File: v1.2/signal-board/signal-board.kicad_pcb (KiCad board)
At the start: 4 copper layers, 73 x 43 mm, 47 parts, among them IC1 74HCT245, J1 Jack-DC, J2 Conn_01x12, J3 JST SM, J4 Conn_01x16, J5 switch_jumpers, J6 switch_jumpers, SW1 SW_MEC_5G, SW2 SW_MEC_5G, U1 TPS63060, U2 ESP32-DEVKITC-32D

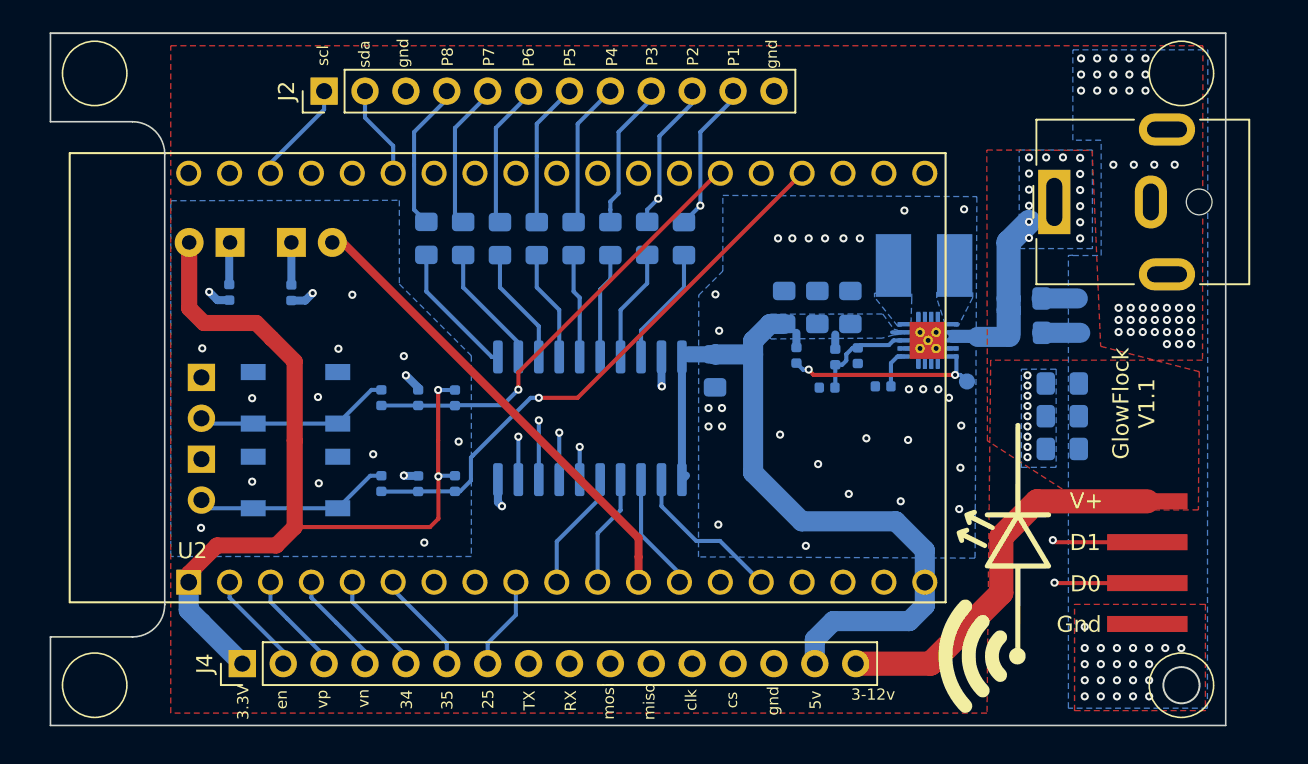
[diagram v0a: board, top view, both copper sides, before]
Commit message: added holes to corners
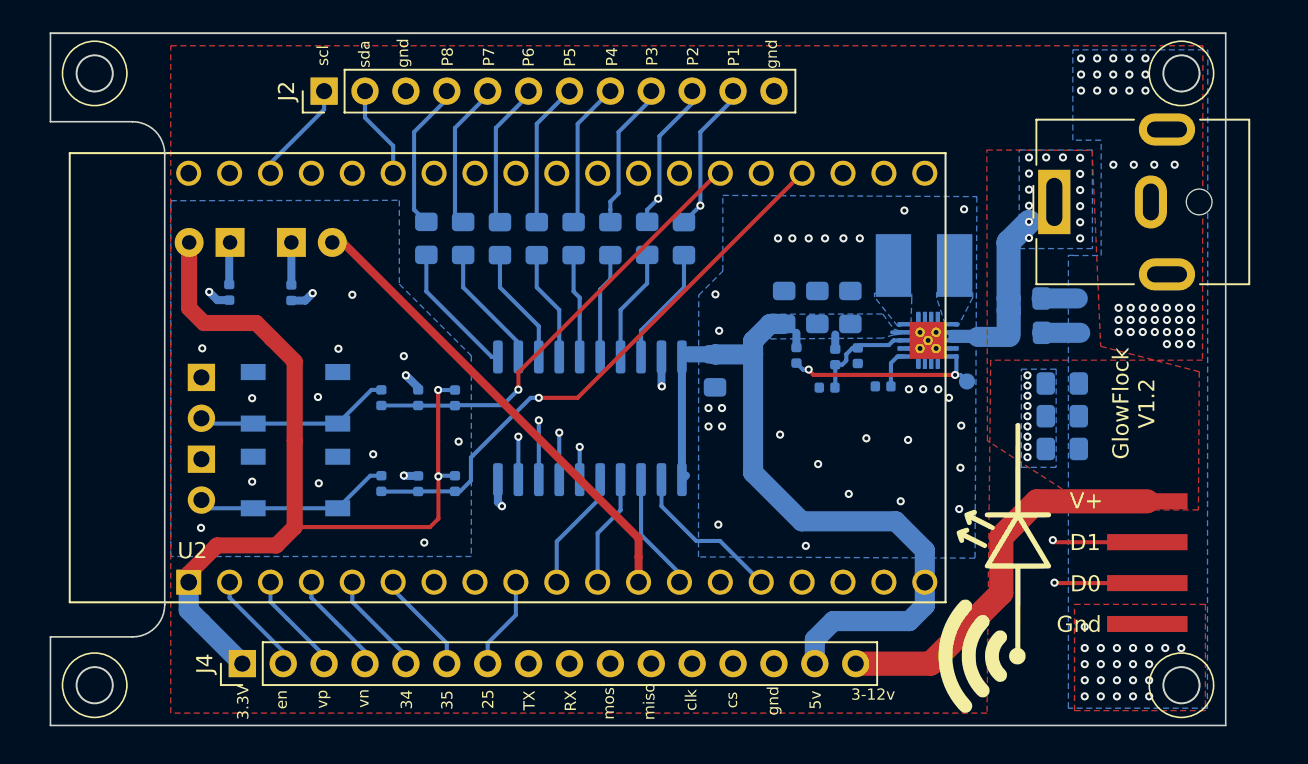
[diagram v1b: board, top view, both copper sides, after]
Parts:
- R1: value 1K -> 1M
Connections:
- U2 pad 16: Net-(U2-Pad16) -> (no net)
- U2 pad 17: Net-(U2-Pad17) -> (no net)
- U2 pad 18: Net-(U2-Pad18) -> (no net)
- U2 pad 36: Net-(U2-Pad36) -> (no net)
- U2 pad 37: Net-(U2-Pad37) -> (no net)
- U2 pad 38: Net-(U2-Pad38) -> (no net)
- U2 pad 7: Net-(U2-Pad7) -> (no net)
- U2 pad 8: Net-(U2-Pad8) -> (no net)
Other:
- outline, holes or cut-outs redrawn
- board text added: "GlowFlock V1.2"
- board text removed: "GlowFlock V1.1"

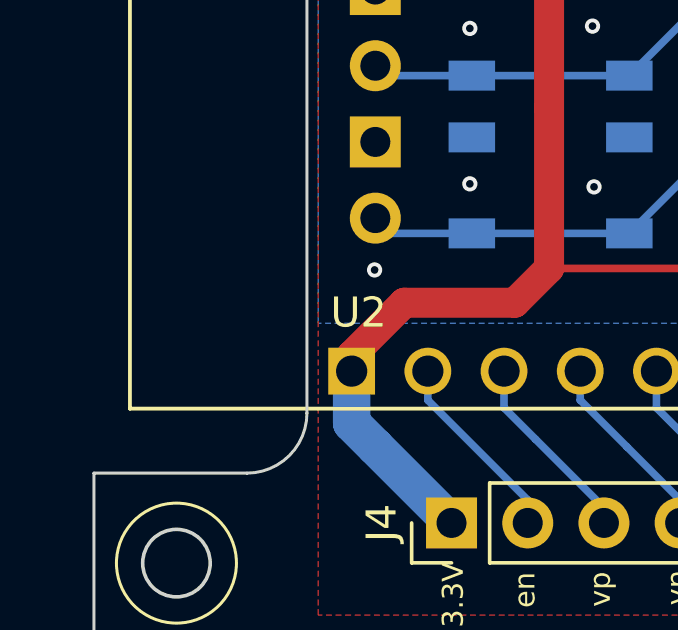
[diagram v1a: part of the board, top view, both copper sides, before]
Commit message: updated symbol and footprint links
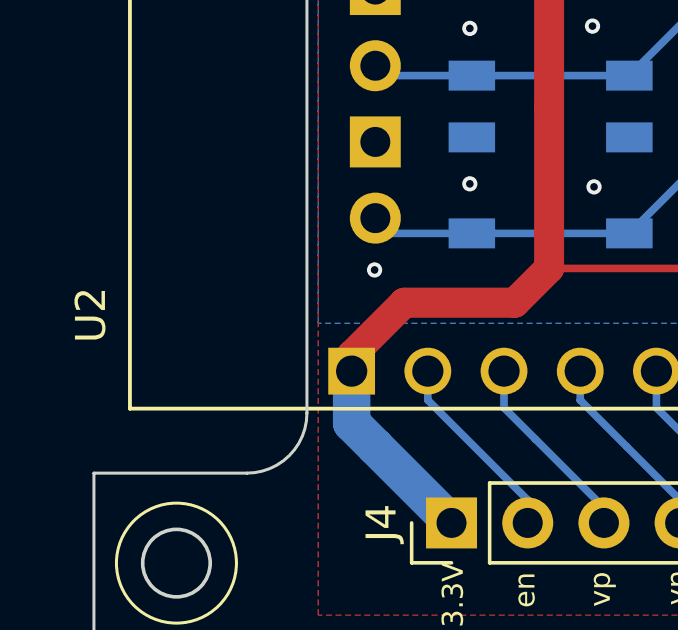
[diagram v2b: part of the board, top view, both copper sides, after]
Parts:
- IC1: footprint 74HCT245:SOIC-20W_7.5x10.0mm_P1.27mm -> GlowFlock footprints:SOIC-20W_7.5x10.0mm_P1.27mm
- SW1, SW2: footprint PTS 647:PTS647SK38SMTR2LFS -> GlowFlock footprints:PTS647SK38SMTR2LFS
- U2: footprint ESP32-DEVKITC-32D:MODULE_ESP32-DEVKITC-32D -> GlowFlock footprints:MODULE_ESP32-DEVKITC-32D
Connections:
- U2 pad 16: (no net) -> Net-(U2-Pad16)
- U2 pad 17: (no net) -> Net-(U2-Pad17)
- U2 pad 18: (no net) -> Net-(U2-Pad18)
- U2 pad 36: (no net) -> Net-(U2-Pad36)
- U2 pad 37: (no net) -> Net-(U2-Pad37)
- U2 pad 38: (no net) -> Net-(U2-Pad38)
- U2 pad 7: (no net) -> Net-(U2-Pad7)
- U2 pad 8: (no net) -> Net-(U2-Pad8)

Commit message: cleanup, new plug
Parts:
- J1: value Jack-DC -> DC Jack - PJ-002AH; footprint Connector_BarrelJack:BarrelJack_CUI_PJ-063AH_Horizontal -> GlowFlock footprints:CUI_PJ-002AH
- turned J1 to 0 degrees
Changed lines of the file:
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@@
   (net 61 "Net-(U2-Pad8)")
   (net 62 "Net-(U2-Pad7)")
+  (net 63 "Net-(J1-Pad3)")
   (module "Connector_PinHeader_2.54mm:PinHeader_1x16_P2.54mm_Vertical" locked (layer "F.Cu")
     (at 109.22 137.16 90)
@@
       (rotate (xyz 0 0 0))
     )
+  )
+  (module "GlowFlock footprints:CUI_PJ-002AH" (layer "F.Cu")
+    (at 159.675 108.475)
+    (property "MANUFACTURER" "CUI INC")
+    (property "STANDARD" "Manufacturer recommendations")
+    (property "Sheet file" "/e_drive/GlowFlock/v1.2/signal-board/signal-board.kicad_sch")
+    (property "Sheet name" "")
+    (attr through_hole)
+    (fp_text reference "J1" (at 2.485118 -6.76532) (layer "F.SilkS")
+      (effects (font (size 1.000047 1.000047) (thickness 0.015)))
+    )
+    (fp_text value "DC Jack - PJ-002AH" (at 6.939165 5.78266) (layer "F.Fab")
+      (effects (font (size 1.001323 1.001323) (thickness 0.015)))
+    )
+    (fp_line (start 13.7 4.5) (end -0.7 4.5) (layer "F.SilkS") (width 0.127))
+    (fp_line (start 13.7 -4.5) (end 13.7 4.5) (layer "F.SilkS") (width 0.127))
+    (fp_line (start -0.7 4.5) (end -0.7 2.65) (layer "F.SilkS") (width 0.127))
+    (fp_line (start -0.7 -2.55) (end -0.7 -4.5) (layer "F.SilkS") (width 0.127))
+    (fp_line (start 5.55 -4.5) (end 13.7 -4.5) (layer "F.SilkS") (width 0.127))
+    (fp_line (start -0.7 -4.5) (end 0.45 -4.5) (layer "F.SilkS") (width 0.127))
+    (fp_circle (center -2 0) (end -1.8 0) (layer "F.SilkS") (width 0.4))
+    (fp_line (start -1.55 2.35) (end -1 2.35) (layer "F.CrtYd") (width 0.05))
+    (fp_line (start 5.55 -4.75) (end 14 -4.75) (layer "F.CrtYd") (width 0.05))
+    (fp_line (start -1 -4.75) (end 0.45 -4.75) (layer "F.CrtYd") (width 0.05))
+    (fp_line (start 5.55 -6.1) (end 5.55 -4.75) (layer "F.CrtYd") (width 0.05))
+    (fp_line (start -1 4.75) (end -1 2.35) (layer "F.CrtYd") (width 0.05))
+    (fp_line (start 14 4.75) (end -1 4.75) (layer "F.CrtYd") (width 0.05))
+    (fp_line (start -1.55 -2.25) (end -1.55 2.35) (layer "F.CrtYd") (width 0.05))
+    (fp_line (start 0.45 -6.1) (end 5.55 -6.1) (layer "F.CrtYd") (width 0.05))
+    (fp_line (start 14 -4.75) (end 14 4.75) (layer "F.CrtYd") (width 0.05))
+    (fp_line (start 0.45 -4.75) (end 0.45 -6.1) (layer "F.CrtYd") (width 0.05))
+    (fp_line (start -1 -2.25) (end -1 -4.75) (layer "F.CrtYd") (width 0.05))
+    (fp_line (start -1 -2.25) (end -1.55 -2.25) (layer "F.CrtYd") (width 0.05))
+    (fp_line (start -0.7 4.5) (end -0.7 -4.5) (layer "F.Fab") (width 0.127))
+    (fp_line (start 13.7 4.5) (end -0.7 4.5) (layer "F.Fab") (width 0.127))
+    (fp_line (start 13.7 -4.5) (end 13.7 4.5) (layer "F.Fab") (width 0.127))
+    (fp_line (start -0.7 -4.5) (end 13.7 -4.5) (layer "F.Fab") (width 0.127))
+    (pad "1" thru_hole oval (at 0 0) (size 2.5 5) (drill oval 1 3.5) (layers *.Cu *.Mask)
+      (net 17 "/3-12v"))
+    (pad "2" thru_hole oval (at 6 0) (size 2.25 4.5) (drill oval 1 3) (layers *.Cu *.Mask)
+      (net 1 "GND"))
+    (pad "3" thru_hole oval (at 3 -4.7) (size 4.5 2.25) (drill oval 3 1) (layers *.Cu *.Mask)
+      (net 63 "Net-(J1-Pad3)"))
   )
   (module "WiFi LED Logo:wifi_to_led_18mm" (layer "F.Cu")
@@
       (offset (xyz 0 0 0))
       (scale (xyz 1 1 1))
-      (rotate (xyz 0 0 0))
-    )
-  )
-  (module "Connector_BarrelJack:BarrelJack_CUI_PJ-063AH_Horizontal" (layer "F.Cu")
-    (at 159.6522 108.4834 90)
-    (descr "Barrel Jack, 2.0mm ID, 5.5mm OD, 24V, 8A, no switch, https://www.cui.com/product/resource/pj-063ah.pdf")
-    (tags "barrel jack cui dc power")
-    (property "DigiKey100" "0.53")
-    (property "DigiKeyPN" "CP-002AH-ND")
-    (property "Sheet file" "/e_drive/GlowFlock/v1.2/signal-board/signal-board.kicad_sch")
-    (property "Sheet name" "")
-    (property "Supplier Part" "PJ-002AH")
-    (zone_connect 2)
-    (attr through_hole)
-    (fp_text reference "J1" (at 0 -2.3 90) (layer "F.SilkS") hide
-      (effects (font (size 1 1) (thickness 0.15)))
-    )
-    (fp_text value "Jack-DC" (at 0 13 90) (layer "F.Fab")
-      (effects (font (size 1 1) (thickness 0.15)))
-    )
-    (fp_text user "${REFERENCE}" (at 0 5.5 90) (layer "F.Fab")
-      (effects (font (size 1 1) (thickness 0.15)))
-    )
-    (fp_line (start -5.11 12.11) (end -5.11 9.05) (layer "F.SilkS") (width 0.12))
-    (fp_line (start 5.11 9.05) (end 5.11 12.11) (layer "F.SilkS") (width 0.12))
-    (fp_line (start 2.3 -1.11) (end 5.11 -1.11) (layer "F.SilkS") (width 0.12))
-    (fp_line (start -5.11 -1.11) (end -2.3 -1.11) (layer "F.SilkS") (width 0.12))
-    (fp_line (start -1 -1.3) (end 1 -1.3) (layer "F.SilkS") (width 0.12))
-    (fp_line (start -5.11 4.95) (end -5.11 -1.11) (layer "F.SilkS") (width 0.12))
-    (fp_line (start 5.11 -1.11) (end 5.11 4.95) (layer "F.SilkS") (width 0.12))
-    (fp_line (start 5.11 12.11) (end -5.11 12.11) (layer "F.SilkS") (width 0.12))
-    (fp_line (start 6 12.5) (end 6 -1.5) (layer "F.CrtYd") (width 0.05))
-    (fp_line (start -6 -1.5) (end -6 12.5) (layer "F.CrtYd") (width 0.05))
-    (fp_line (start 6 -1.5) (end -6 -1.5) (layer "F.CrtYd") (width 0.05))
-    (fp_line (start -6 12.5) (end 6 12.5) (layer "F.CrtYd") (width 0.05))
-    (fp_line (start 5 -1) (end 5 12) (layer "F.Fab") (width 0.1))
-    (fp_line (start -5 12) (end -5 -1) (layer "F.Fab") (width 0.1))
-    (fp_line (start 1 -1) (end 5 -1) (layer "F.Fab") (width 0.1))
-    (fp_line (start -1 -1) (end 0 0) (layer "F.Fab") (width 0.1))
-    (fp_line (start 0 0) (end 1 -1) (layer "F.Fab") (width 0.1))
-    (fp_line (start -5 -1) (end -1 -1) (layer "F.Fab") (width 0.1))
-    (fp_line (start 5 12) (end -5 12) (layer "F.Fab") (width 0.1))
-    (pad "" np_thru_hole circle (at 0 9 90) (size 1.6 1.6) (drill 1.6) (layers *.Cu *.Mask)
-      (zone_connect 2))
-    (pad "1" thru_hole rect (at 0 0 90) (size 4 2) (drill oval 3 1) (layers *.Cu *.Mask)
-      (net 17 "/3-12v") (zone_connect 2))
-    (pad "2" thru_hole oval (at 0 6 90) (size 3.3 2) (drill oval 2.3 1) (layers *.Cu *.Mask)
-      (net 1 "GND") (zone_connect 2))
-    (pad "MP" thru_hole oval (at 4.5 7 90) (size 2 3.5) (drill oval 1 2.5) (layers *.Cu *.Mask)
-      (zone_connect 2))
-    (pad "MP" thru_hole oval (at -4.5 7 90) (size 2 3.5) (drill oval 1 2.5) (layers *.Cu *.Mask)
-      (zone_connect 2))
-    (model "${KISYS3DMOD}/Connector_BarrelJack.3dshapes/BarrelJack_CUI_PJ-063AH_Horizontal.wrl"
-      (offset (xyz 0 0 0))
-      (scale (xyz 1 1 1))

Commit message: updates for v1.2
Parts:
- added 5V_SW1: TestPoint, TestPoint:TestPoint_Pad_D1.0mm, B.Cu at (145.9, 129.3)
- added C14: 10uF, Capacitor_SMD:C_0805_2012Metric_Pad1.15x1.40mm_HandSolder, B.Cu at (154.3, 100.3)
- added C15: 100pF, Capacitor_SMD:C_0805_2012Metric_Pad1.15x1.40mm_HandSolder, B.Cu at (150.4, 103.5)
- added C16: 22uF, Capacitor_SMD:C_0805_2012Metric_Pad1.15x1.40mm_HandSolder, B.Cu at (149.5, 100.3)
- added C17: 22uF, Capacitor_SMD:C_0805_2012Metric_Pad1.15x1.40mm_HandSolder, B.Cu at (151.9, 100.3)
- added D3: D, Diode_SMD:D_0603_1608Metric, B.Cu at (160.7, 132.1)
- added D4: D, Diode_SMD:D_0603_1608Metric, B.Cu at (160.7, 129.6)
- added F1: 3A Fuse, Fuse:Fuse_1206_3216Metric, B.Cu at (158.8, 100.7)
- added R18: 0, Resistor_SMD:R_0402_1005Metric, B.Cu at (155.3, 109.2)
- added R19: 4.7k, Resistor_SMD:R_0402_1005Metric, B.Cu at (156.4, 101.0)
- added R20: 300K, Resistor_SMD:R_0402_1005Metric, B.Cu at (148.9, 119.6)
- added R21: 300K, Resistor_SMD:R_0402_1005Metric, B.Cu at (148.9, 120.8)
- added R22: 15, Resistor_SMD:R_0402_1005Metric, B.Cu at (143.8, 126.8)
- added R23: 0, Resistor_SMD:R_0402_1005Metric, B.Cu at (156.9, 114.1)
- added R24: NP, Resistor_SMD:R_0402_1005Metric, B.Cu at (156.9, 116.3)
- added TP1: TestPoint, TestPoint:TestPoint_Pad_D1.0mm, B.Cu at (139.8, 110.5)
- added TP10: TestPoint, TestPoint:TestPoint_Pad_D1.0mm, B.Cu at (140.0, 114.4)
- added TP11: TestPoint, TestPoint:TestPoint_Pad_D1.0mm, B.Cu at (150.4, 127.1)
- added TP2: TestPoint, TestPoint:TestPoint_Pad_D1.0mm, B.Cu at (153.2, 124.5)
- added TP2-3: TestPoint, TestPoint:TestPoint_Pad_D1.0mm, B.Cu at (147.3, 108.7)
- added TP3: TestPoint, TestPoint:TestPoint_Pad_D1.0mm, B.Cu at (147.0, 101.2)
- added TP4: TestPoint, TestPoint:TestPoint_Pad_D1.0mm, B.Cu at (154.3, 117.9)
- added TP6: TestPoint, TestPoint:TestPoint_Pad_D1.0mm, B.Cu at (154.3, 122.8)
- added TP8: TestPoint, TestPoint:TestPoint_Pad_D1.0mm, B.Cu at (150.3, 124.6)
- added TP9: TestPoint, TestPoint:TestPoint_Pad_D1.0mm, B.Cu at (143.7, 124.4)
- added TP_GND1: TestPoint, TestPoint:TestPoint_Pad_D1.0mm, F.Cu at (104.5, 100.6)
- added TP_GND2: TestPoint, TestPoint:TestPoint_Pad_D1.0mm, F.Cu at (104.7, 138.6)
- added TP_GND3: TestPoint, TestPoint:TestPoint_Pad_D1.0mm, B.Cu at (163.7, 100.3)
- added TP_GND4: TestPoint, TestPoint:TestPoint_Pad_D1.0mm, B.Cu at (104.4, 100.6)
- added TP_GND5: TestPoint, TestPoint:TestPoint_Pad_D1.0mm, B.Cu at (104.7, 138.6)
- added TP_GND6: TestPoint, TestPoint:TestPoint_Pad_D1.0mm, F.Cu at (163.7, 100.3)
- added TP_GND7: TestPoint, TestPoint:TestPoint_Pad_D1.0mm, B.Cu at (161.2, 139.9)
- added TP_GND8: TestPoint, TestPoint:TestPoint_Pad_D1.0mm, F.Cu at (161.2, 139.9)
- added U3: TPS2553DBVR, Package_TO_SOT_SMD:SOT-23-6_Handsoldering, B.Cu at (147.0, 125.8)
- added U4: TPS22810DBVR, Package_TO_SOT_SMD:SOT-23-6_Handsoldering, B.Cu at (155.5, 104.9)
- added U5: 74LVC1G32, Package_TO_SOT_SMD:SOT-353_SC-70-5_Handsoldering, B.Cu at (153.6, 115.2)
- R1: value 1M -> 300K
- R2: value 110K -> 100K
- moved C2 9.05 mm to (151.5, 110.2), turned to -90 degrees
- moved L1 8.30 mm to (143.3, 112.6), turned to -90 degrees
- moved C10 7.79 mm to (139.1, 126.7), turned to 90 degrees
- moved C3 7.52 mm to (151.5, 112.8), turned to 0 degrees
- moved C5 6.91 mm to (145.9, 121.3), turned to 180 degrees
- moved R3 6.58 mm to (148.9, 122.0), turned to 0 degrees
- moved U1 6.15 mm to (147.9, 112.3), turned to -90 degrees
- moved C1 6.04 mm to (153.6, 110.1), turned to -90 degrees
- moved C4 5.16 mm to (148.9, 116.1), turned to 0 degrees
- moved C11 5.16 mm to (162.4, 115.1)
- moved C12 5.16 mm to (162.4, 117.1)
- moved C13 5.16 mm to (162.4, 119.2)
- moved C6 4.27 mm to (145.9, 119.2), turned to 180 degrees
- moved R1 2.82 mm to (148.9, 118.4), turned to 0 degrees
- moved C7 2.39 mm to (145.9, 117.1), turned to 180 degrees
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- renumbered TP1 to TP5
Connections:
- net Net-(R3-Pad2) renamed /5V_Out_PG
- C1 pad 1: /3-12v -> /3-12V_FUSED_SW
- C11 pad 1: /3-12v -> /3-12V_UNFUSED
- C12 pad 1: /3-12v -> /3-12V_UNFUSED
- C13 pad 1: /3-12v -> /3-12V_UNFUSED
- C2 pad 1: /3-12v -> /3-12V_FUSED_SW
- C4 pad 1: Net-(C4-Pad1) -> /TPS_FEEDBACK
- C5 pad 1: +5V -> VCC
- C6 pad 1: +5V -> VCC
- C7 pad 1: +5V -> VCC
- J1 pad 1: /3-12v -> /3-12V_UNFUSED
- J1 pad 3: Net-(J1-Pad3) -> GND
- J3 pad 1: /3-12v -> /3-12V_UNFUSED
- J4 pad 16: /3-12v -> /3-12V_UNFUSED
- R1 pad 1: +5V -> /TPS_FEEDBACK
- R1 pad 2: Net-(C4-Pad1) -> Net-(R1-Pad2)
- R2 pad 1: Net-(C4-Pad1) -> /TPS_FEEDBACK
- R3 pad 1: +5V -> VCC
- U1 pad 2: /3-12v -> /3-12V_FUSED_SW
- U1 pad 3: /3-12v -> /3-12V_FUSED_SW
- U1 pad 8: Net-(C4-Pad1) -> /TPS_FEEDBACK
- U1 pad 9: +5V -> VCC
- U2 pad 16: Net-(U2-Pad16) -> (no net)
- U2 pad 17: Net-(U2-Pad17) -> (no net)
- U2 pad 18: Net-(U2-Pad18) -> (no net)
- U2 pad 36: Net-(U2-Pad36) -> (no net)
- U2 pad 37: Net-(U2-Pad37) -> (no net)
- U2 pad 38: Net-(U2-Pad38) -> (no net)
- U2 pad 7: Net-(U2-Pad7) -> (no net)
- U2 pad 8: Net-(U2-Pad8) -> (no net)
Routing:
- net /3-12v: track 37.0 -> 0.00 mm, vias 23 -> 0
- net /3-12V_UNFUSED: track 0.00 -> 28.2 mm, vias 0 -> 24
- net /EN_2553: track 0.00 -> 24.0 mm
- net VCC: track 0.00 -> 20.3 mm, vias 0 -> 2
- net /5V_Out_PG: track 12.3 -> 27.4 mm, vias 2 -> 4
- net /TPS_FEEDBACK: track 0.00 -> 15.0 mm, vias 0 -> 2
- net /3-12V_FUSED_SW: track 0.00 -> 14.3 mm
- net Net-(C16-Pad1): track 0.00 -> 13.7 mm, vias 0 -> 2
- net Net-(C3-Pad1): track 2.45 -> 14.0 mm, vias 0 -> 2
- net GND: track 18.4 -> 29.4 mm, vias 113 -> 126
- net +5V: track 50.2 -> 39.5 mm
- net Net-(C15-Pad1): track 0.00 -> 10.3 mm, vias 0 -> 2
- net /3-12V_FUSED: track 0.00 -> 7.94 mm
- net Net-(C4-Pad1): track 6.31 -> 0.00 mm
- net Net-(R22-Pad1): track 0.00 -> 4.71 mm
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- added copper zone on B.Cu, net /3-12V_UNFUSED
- added copper zone on F.Cu, net /3-12V_UNFUSED
- added copper zone on In1.Cu, net GND
- added copper zone on B.Cu, net VCC
- removed copper zone on B.Cu, net +5V
- removed copper zone on B.Cu, net /3-12v
- removed copper zone on F.Cu, net /3-12v
